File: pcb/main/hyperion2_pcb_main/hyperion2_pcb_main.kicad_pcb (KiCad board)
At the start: 2 copper layers, 6 parts, among them J1 RJ45_LED_Shielded, T1 H1102NLT, U1 ESP32-S3-WROOM-1U-N16R8, U2 MAX3488ECSA_, U3 PCA9685PW_118, U4 W5500

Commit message: placed more components
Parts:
- added J2: USB_C_Receptacle_USB2.0, Connector_USB:USB_C_Receptacle_G-Switch_GT-USB-7010ASV, F.Cu at (177.8, 27.9)
- added J3: Barrel_Jack, powerpole:POWERPOLEPCBMOUNT, F.Cu at (147.8, 124.0)
- added J4: Barrel_Jack, Connector_JST:JST_XH_B2B-XH-AM_1x02_P2.50mm_Vertical, F.Cu at (160.1, 106.7)
- added Q1: NCV8401, Package_TO_SOT_SMD:TO-252-2, F.Cu at (109.2, 54.9)
- added Q10: NCV8401, Package_TO_SOT_SMD:TO-252-2, F.Cu at (185.4, 85.9)
- added Q11: NCV8401, Package_TO_SOT_SMD:TO-252-2, F.Cu at (185.4, 94.0)
- added Q12: NCV8401, Package_TO_SOT_SMD:TO-252-2, F.Cu at (185.4, 102.0)
- added Q2: NCV8401, Package_TO_SOT_SMD:TO-252-2, F.Cu at (109.2, 65.0)
- added Q3: NCV8401, Package_TO_SOT_SMD:TO-252-2, F.Cu at (108.0, 75.2)
- added Q4: NCV8401, Package_TO_SOT_SMD:TO-252-2, F.Cu at (108.8, 86.4)
- added Q5: NCV8401, Package_TO_SOT_SMD:TO-252-2, F.Cu at (107.1, 96.6)
- added Q6: NCV8401, Package_TO_SOT_SMD:TO-252-2, F.Cu at (107.1, 104.7)
- added Q7: NCV8401, Package_TO_SOT_SMD:TO-252-2, F.Cu at (185.4, 55.9)
- added Q8: NCV8401, Package_TO_SOT_SMD:TO-252-2, F.Cu at (185.4, 63.9)
- added Q9: NCV8401, Package_TO_SOT_SMD:TO-252-2, F.Cu at (185.4, 77.9)
- added U5: LMR16006YQ5, Package_TO_SOT_SMD:SOT-23-6, F.Cu at (138.6, 93.0)
- added U6: SN74HCT245PWR, SN74HCT245PWR:SOP65P640X120-20N, F.Cu at (142.2, 45.7)
- moved U1 39.9 mm to (138.0, 60.3), turned to 90 degrees
- moved U3 31.7 mm to (137.5, 83.4), turned to -90 degrees
- moved U2 6.99 mm to (111.8, 43.2)
- moved U4 6.78 mm to (159.1, 61.9)
- moved T1 4.90 mm to (159.2, 49.1), turned to 90 degrees
- moved J1 1.85 mm to (107.7, 31.2)
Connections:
- J1 pad 37: unconnected-(J1D-1-Pad37) -> Net-(J1D-1)
- J1 pad 38: unconnected-(J1D-2-Pad38) -> Net-(J1D-2)
- J1 pad 39: unconnected-(J1D-3-Pad39) -> Net-(J1D-3)
- J1 pad 42: unconnected-(J1D-6-Pad42) -> Net-(J1D-6)
- T1 pad 1: unconnected-(T1-Pad1) -> Net-(U4-TXP)
- T1 pad 11: unconnected-(T1-Pad11) -> Net-(J1D-3)
- T1 pad 14: unconnected-(T1-Pad14) -> Net-(J1D-2)
- T1 pad 16: unconnected-(T1-Pad16) -> Net-(J1D-1)
- T1 pad 3: unconnected-(T1-Pad3) -> Net-(U4-TXN)
- T1 pad 6: unconnected-(T1-Pad6) -> Net-(U4-RXP)
- T1 pad 8: unconnected-(T1-Pad8) -> Net-(U4-RXN)
- T1 pad 9: unconnected-(T1-Pad9) -> Net-(J1D-6)
- U1 pad 13: unconnected-(U1-IO19-Pad13) -> Net-(U1-IO19)
- U1 pad 14: unconnected-(U1-IO20-Pad14) -> Net-(U1-IO20)
- U1 pad 17: unconnected-(U1-IO9-Pad17) -> Net-(U1-IO9)
- U1 pad 18: unconnected-(U1-IO10-Pad18) -> Net-(U1-IO10)
- U1 pad 19: unconnected-(U1-IO11-Pad19) -> Net-(U1-IO11)
- U1 pad 20: unconnected-(U1-IO12-Pad20) -> Net-(U1-IO12)
- U1 pad 21: unconnected-(U1-IO13-Pad21) -> Net-(U1-IO13)
- U1 pad 22: unconnected-(U1-IO14-Pad22) -> Net-(U1-IO14)
- U4 pad 1: unconnected-(U4-TXN-Pad1) -> Net-(U4-TXN)
- U4 pad 2: unconnected-(U4-TXP-Pad2) -> Net-(U4-TXP)
- U4 pad 32: unconnected-(U4-~{SCSN}-Pad32) -> Net-(U1-IO9)
- U4 pad 33: unconnected-(U4-SCLK-Pad33) -> Net-(U1-IO10)
- U4 pad 34: unconnected-(U4-MISO-Pad34) -> Net-(U1-IO11)
- U4 pad 35: unconnected-(U4-MOSI-Pad35) -> Net-(U1-IO12)
- U4 pad 36: unconnected-(U4-~{INTN}-Pad36) -> Net-(U1-IO13)
- U4 pad 37: unconnected-(U4-~{RSTN}-Pad37) -> Net-(U1-IO14)
- U4 pad 5: unconnected-(U4-RXN-Pad5) -> Net-(U4-RXN)
- U4 pad 6: unconnected-(U4-RXP-Pad6) -> Net-(U4-RXP)
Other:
- board outline added: 92.5 x 100 mm
- copper layers 2 -> 4

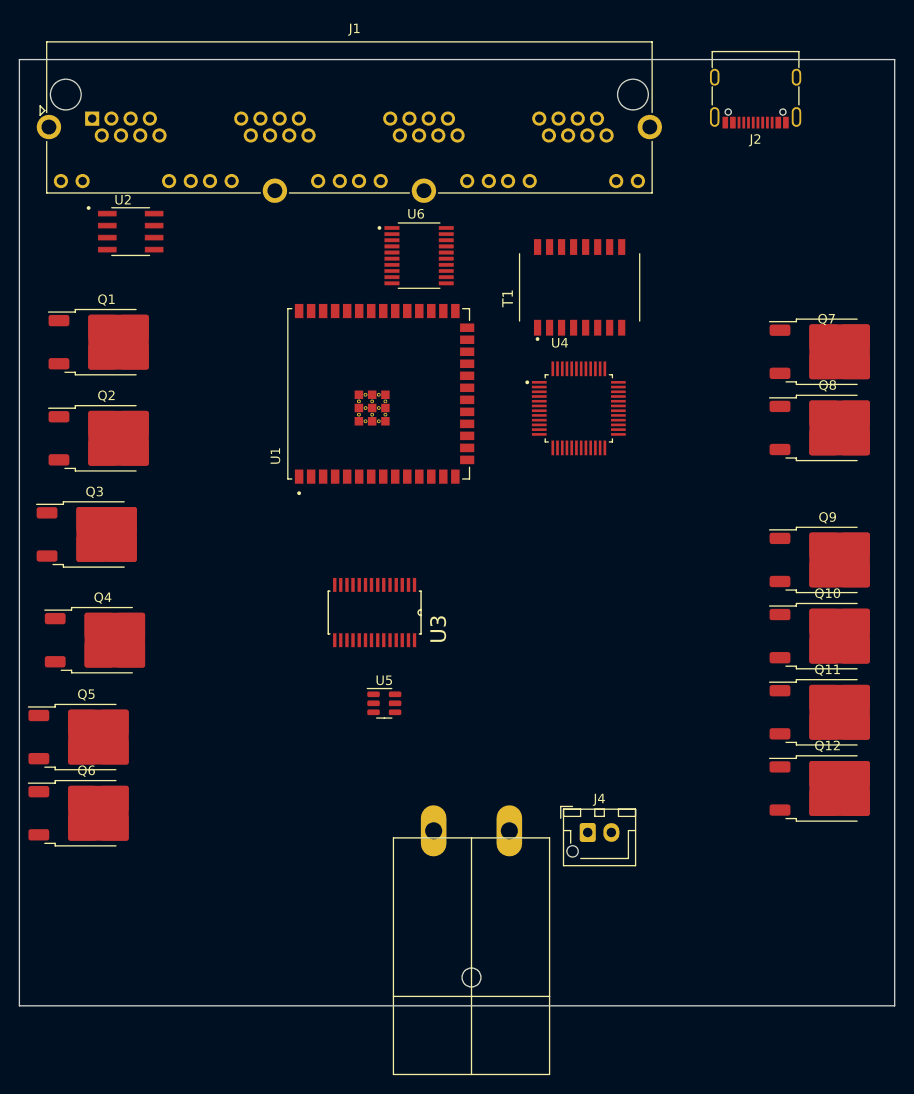
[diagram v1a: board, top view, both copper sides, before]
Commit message: board size, placement of connectors
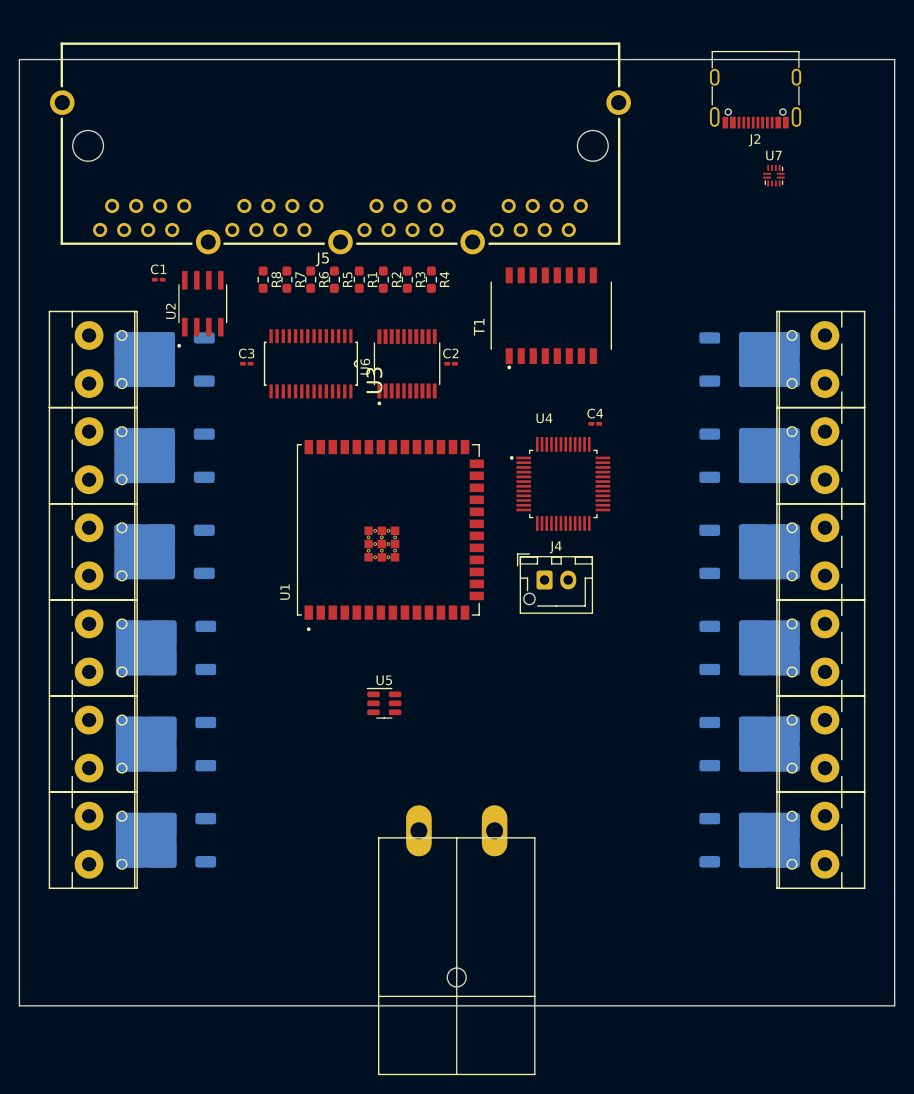
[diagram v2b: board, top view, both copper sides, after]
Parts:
- added C1: 100nF, Capacitor_SMD:C_0201_0603Metric_Pad0.64x0.40mm_HandSolder, F.Cu at (114.7, 48.3)
- added C2: 100nF, Capacitor_SMD:C_0201_0603Metric_Pad0.64x0.40mm_HandSolder, F.Cu at (145.6, 57.1)
- added C3: 100nF, Capacitor_SMD:C_0201_0603Metric_Pad0.64x0.40mm_HandSolder, F.Cu at (124.0, 57.1)
- added C4: 100nF, Capacitor_SMD:C_0201_0603Metric_Pad0.64x0.40mm_HandSolder, F.Cu at (160.9, 63.5)
- added J10: Screw_Terminal_01x02, con_wago_508_w237_132Pluggable:CON-WAGO-508_W237-132PLUGGABLE, F.Cu at (108.0, 107.5)
- added J12: Screw_Terminal_01x02, con_wago_508_w237_132Pluggable:CON-WAGO-508_W237-132PLUGGABLE, F.Cu at (108.0, 56.7)
- added J13: Screw_Terminal_01x02, con_wago_508_w237_132Pluggable:CON-WAGO-508_W237-132PLUGGABLE, F.Cu at (184.5, 107.5)
- added J14: Screw_Terminal_01x02, con_wago_508_w237_132Pluggable:CON-WAGO-508_W237-132PLUGGABLE, F.Cu at (184.5, 97.3)
- added J15: Screw_Terminal_01x02, con_wago_508_w237_132Pluggable:CON-WAGO-508_W237-132PLUGGABLE, F.Cu at (184.5, 77.0)
- added J16: Screw_Terminal_01x02, con_wago_508_w237_132Pluggable:CON-WAGO-508_W237-132PLUGGABLE, F.Cu at (184.5, 66.9)
- added J17: Screw_Terminal_01x02, con_wago_508_w237_132Pluggable:CON-WAGO-508_W237-132PLUGGABLE, F.Cu at (184.5, 56.7)
- added J5: 8P8C_Shielded, ethernet_4_port:CONN-TH_DS1129-02-S80BP, F.Cu at (133.9, 36.9)
- added J6: Screw_Terminal_01x02, con_wago_508_w237_132Pluggable:CON-WAGO-508_W237-132PLUGGABLE, F.Cu at (108.0, 66.9)
- added J7: Screw_Terminal_01x02, con_wago_508_w237_132Pluggable:CON-WAGO-508_W237-132PLUGGABLE, F.Cu at (108.0, 77.0)
- added J8: Screw_Terminal_01x02, con_wago_508_w237_132Pluggable:CON-WAGO-508_W237-132PLUGGABLE, F.Cu at (108.0, 87.2)
- added J9: Screw_Terminal_01x02, con_wago_508_w237_132Pluggable:CON-WAGO-508_W237-132PLUGGABLE, F.Cu at (108.0, 97.3)
- added R1: 100R, Resistor_SMD:R_0603_1608Metric_Pad0.98x0.95mm_HandSolder, F.Cu at (135.9, 48.3)
- added R2: 100R, Resistor_SMD:R_0603_1608Metric_Pad0.98x0.95mm_HandSolder, F.Cu at (138.5, 48.3)
- added R3: 100R, Resistor_SMD:R_0603_1608Metric_Pad0.98x0.95mm_HandSolder, F.Cu at (141.0, 48.3)
- added R4: 100R, Resistor_SMD:R_0603_1608Metric_Pad0.98x0.95mm_HandSolder, F.Cu at (143.5, 48.3)
- added R5: 100R, Resistor_SMD:R_0603_1608Metric_Pad0.98x0.95mm_HandSolder, F.Cu at (133.3, 48.3)
- added R6: 100R, Resistor_SMD:R_0603_1608Metric_Pad0.98x0.95mm_HandSolder, F.Cu at (130.8, 48.3)
- added R7: 100R, Resistor_SMD:R_0603_1608Metric_Pad0.98x0.95mm_HandSolder, F.Cu at (128.3, 48.3)
- added R8: 100R, Resistor_SMD:R_0603_1608Metric_Pad0.98x0.95mm_HandSolder, F.Cu at (125.8, 48.3)
- added U7: TUSB320, Package_DFN_QFN:Texas_X2QFN-12_1.6x1.6mm_P0.4mm, F.Cu at (179.7, 37.3)
- J1: value RJ45_LED_Shielded -> Screw_Terminal_01x02; footprint Connector_RJ:RJ45_Amphenol_RJHSE538X-04 -> con_wago_508_w237_132Pluggable:CON-WAGO-508_W237-132PLUGGABLE
- Q1, Q10, Q11, Q12, Q2, Q3, Q4, Q5, Q6, Q7, Q8, Q9: moved to B.Cu
- moved J1 95.0 mm to (184.5, 87.2), turned to 90 degrees
- moved Q7 52.2 mm to (178.0, 107.5)
- moved Q12 45.9 mm to (178.0, 56.7)
- moved Q8 34.2 mm to (178.0, 97.3)
- moved Q11 28.1 mm to (178.0, 66.9)
- moved U3 27.1 mm to (130.8, 57.1)
- moved J4 27.1 mm to (155.5, 80.0)
- moved U1 14.4 mm to (139.0, 74.7)
- moved Q9 11.9 mm to (178.0, 87.2)
- moved Q10 11.6 mm to (178.0, 77.0)
- moved U6 11.5 mm to (141.0, 57.1), turned to 90 degrees
- moved U2 10.8 mm to (119.4, 50.8), turned to 90 degrees
- moved U4 8.16 mm to (157.5, 69.8)
- moved Q6 8.08 mm to (114.7, 107.5), turned to 180 degrees
- moved Q5 7.60 mm to (114.7, 97.3), turned to 180 degrees
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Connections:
- J1 pad 1: unconnected-(J1-Pad1) -> VDD
- J1 pad 2: unconnected-(J1-Pad2) -> Net-(J1-Pin_2)
- J2 pad A5: unconnected-(J2-CC1-PadA5) -> Net-(J2-CC1)
- J2 pad B5: unconnected-(J2-CC2-PadB5) -> Net-(J2-CC2)
- J4 pad 1: unconnected-(J4-Pad1) -> VDD
- J4 pad 2: unconnected-(J4-Pad2) -> GND
- Q1 pad 3: unconnected-(Q1-S-Pad3) -> GND
- Q10 pad 3: unconnected-(Q10-S-Pad3) -> GND
- Q11 pad 3: unconnected-(Q11-S-Pad3) -> GND
- Q12 pad 3: unconnected-(Q12-S-Pad3) -> GND
- Q2 pad 3: unconnected-(Q2-S-Pad3) -> GND
- Q3 pad 3: unconnected-(Q3-S-Pad3) -> GND
- Q4 pad 3: unconnected-(Q4-S-Pad3) -> GND
- Q5 pad 3: unconnected-(Q5-S-Pad3) -> GND
- Q6 pad 3: unconnected-(Q6-S-Pad3) -> GND
- Q7 pad 3: unconnected-(Q7-S-Pad3) -> GND
- Q8 pad 3: unconnected-(Q8-S-Pad3) -> GND
- Q9 pad 2: Net-(Q9-D-Pad2) -> Net-(J1-Pin_2)
- Q9 pad 3: unconnected-(Q9-S-Pad3) -> GND
- T1 pad 11: Net-(J1D-3) -> Net-(J5-PadA3)
- T1 pad 14: Net-(J1D-2) -> Net-(J5-PadA2)
- T1 pad 16: Net-(J1D-1) -> Net-(J5-PadA1)
- T1 pad 9: Net-(J1D-6) -> Net-(J5-PadA6)
- U2 pad 1: unconnected-(U2-VCC-Pad1) -> +3V3
- U2 pad 2: unconnected-(U2-RO-Pad2) -> DMX_RX
- U2 pad 3: unconnected-(U2-DI-Pad3) -> DMX_TX
- U2 pad 4: unconnected-(U2-GND-Pad4) -> GND
- U2 pad 5: unconnected-(U2-Y-Pad5) -> /DMXY
- U2 pad 6: unconnected-(U2-Z-Pad6) -> /DMXZ
- U2 pad 7: unconnected-(U2-B-Pad7) -> /DMXB
- U2 pad 8: unconnected-(U2-A-Pad8) -> /DMXA
- U6 pad 1: unconnected-(U6-DIR-Pad1) -> +5V
- U6 pad 10: unconnected-(U6-GND-Pad10) -> GND
- U6 pad 11: unconnected-(U6-B8-Pad11) -> Net-(U6-B8)
- U6 pad 12: unconnected-(U6-B7-Pad12) -> Net-(U6-B7)
- U6 pad 13: unconnected-(U6-B6-Pad13) -> Net-(U6-B6)
- U6 pad 14: unconnected-(U6-B5-Pad14) -> Net-(U6-B5)
- U6 pad 15: unconnected-(U6-B4-Pad15) -> Net-(U6-B4)
- U6 pad 16: unconnected-(U6-B3-Pad16) -> Net-(U6-B3)
- U6 pad 17: unconnected-(U6-B2-Pad17) -> Net-(U6-B2)
- U6 pad 18: unconnected-(U6-B1-Pad18) -> Net-(U6-B1)
- U6 pad 19: unconnected-(U6-~{OE}-Pad19) -> GND
- U6 pad 2: unconnected-(U6-A1-Pad2) -> OCTOWS8
- U6 pad 20: unconnected-(U6-VCC-Pad20) -> +5V
- U6 pad 3: unconnected-(U6-A2-Pad3) -> OCTOWS7
- U6 pad 4: unconnected-(U6-A3-Pad4) -> OCTOWS6
- U6 pad 5: unconnected-(U6-A4-Pad5) -> OCTOWS5
- U6 pad 6: unconnected-(U6-A5-Pad6) -> OCTOWS4
- U6 pad 7: unconnected-(U6-A6-Pad7) -> OCTOWS3
- U6 pad 8: unconnected-(U6-A7-Pad8) -> OCTOWS2
- U6 pad 9: unconnected-(U6-A8-Pad9) -> OCTOWS1

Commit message: panel connector
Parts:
- added J11: Panel, Connector_PinHeader_2.54mm:PinHeader_2x05_P2.54mm_Vertical, F.Cu at (185.3, 45.5)
- added J18: Barrel_Jack, Connector_JST:JST_XH_B2B-XH-AM_1x02_P2.50mm_Vertical, F.Cu at (155.0, 88.5)
- moved U7 12.8 mm to (168.9, 30.5)
- turned J4 to -90 degrees

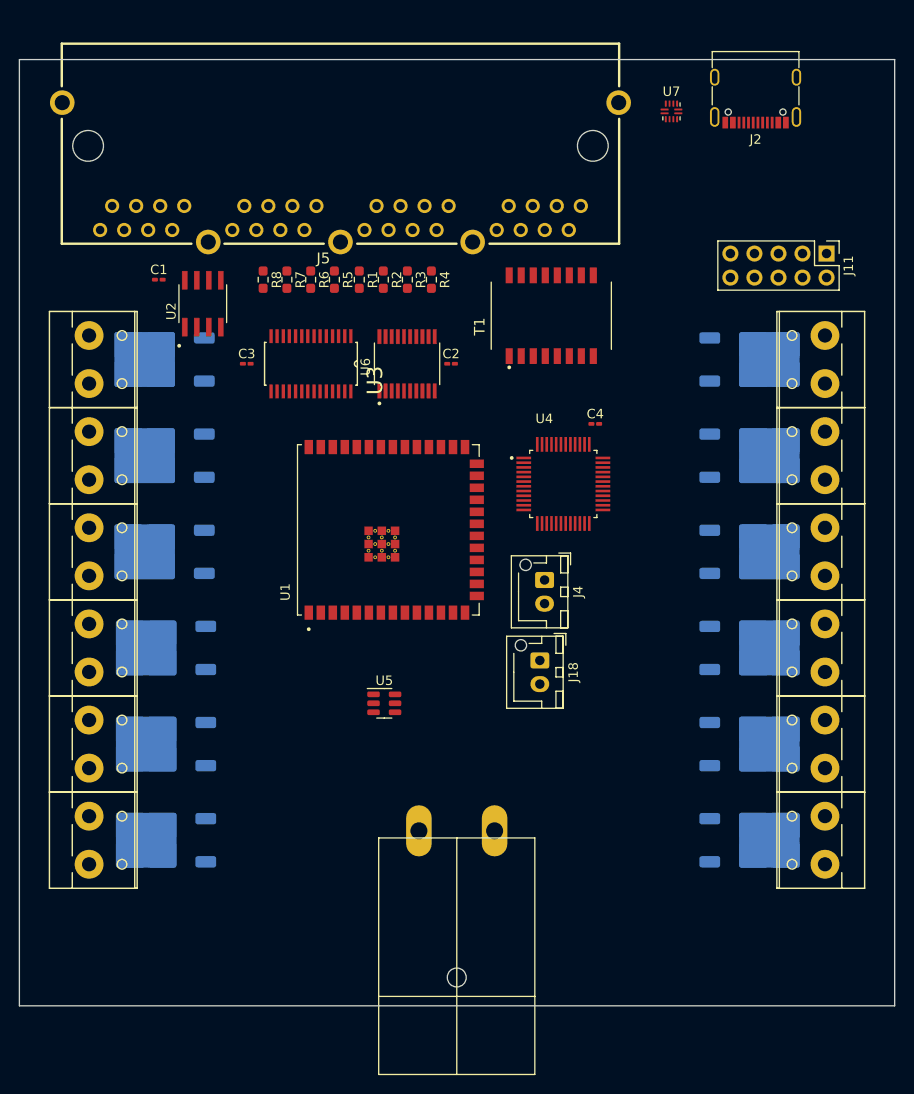
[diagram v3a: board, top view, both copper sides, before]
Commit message: exact alignment with v1 pcb
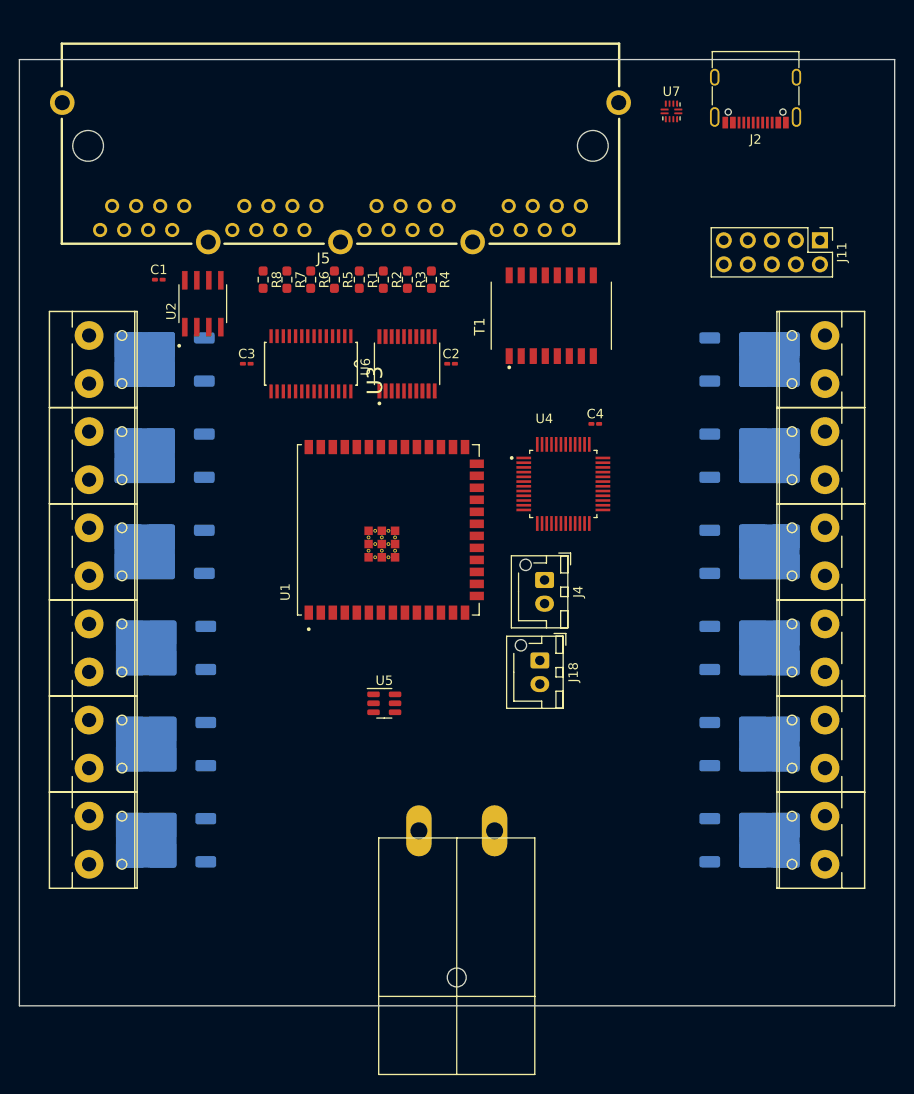
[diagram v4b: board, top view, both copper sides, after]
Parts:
- moved J11 1.57 mm to (184.6, 44.1)
